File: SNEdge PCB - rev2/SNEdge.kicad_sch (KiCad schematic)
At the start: 37 parts, among them J10 R_O, J2 R_E, J3 B_E, J4 G_E, J5 G_IN, J6 B_IN, J7 R_IN, J8 G_O, J9 B_O, U1 THS7374, U3 MIC5205-5.0YM5

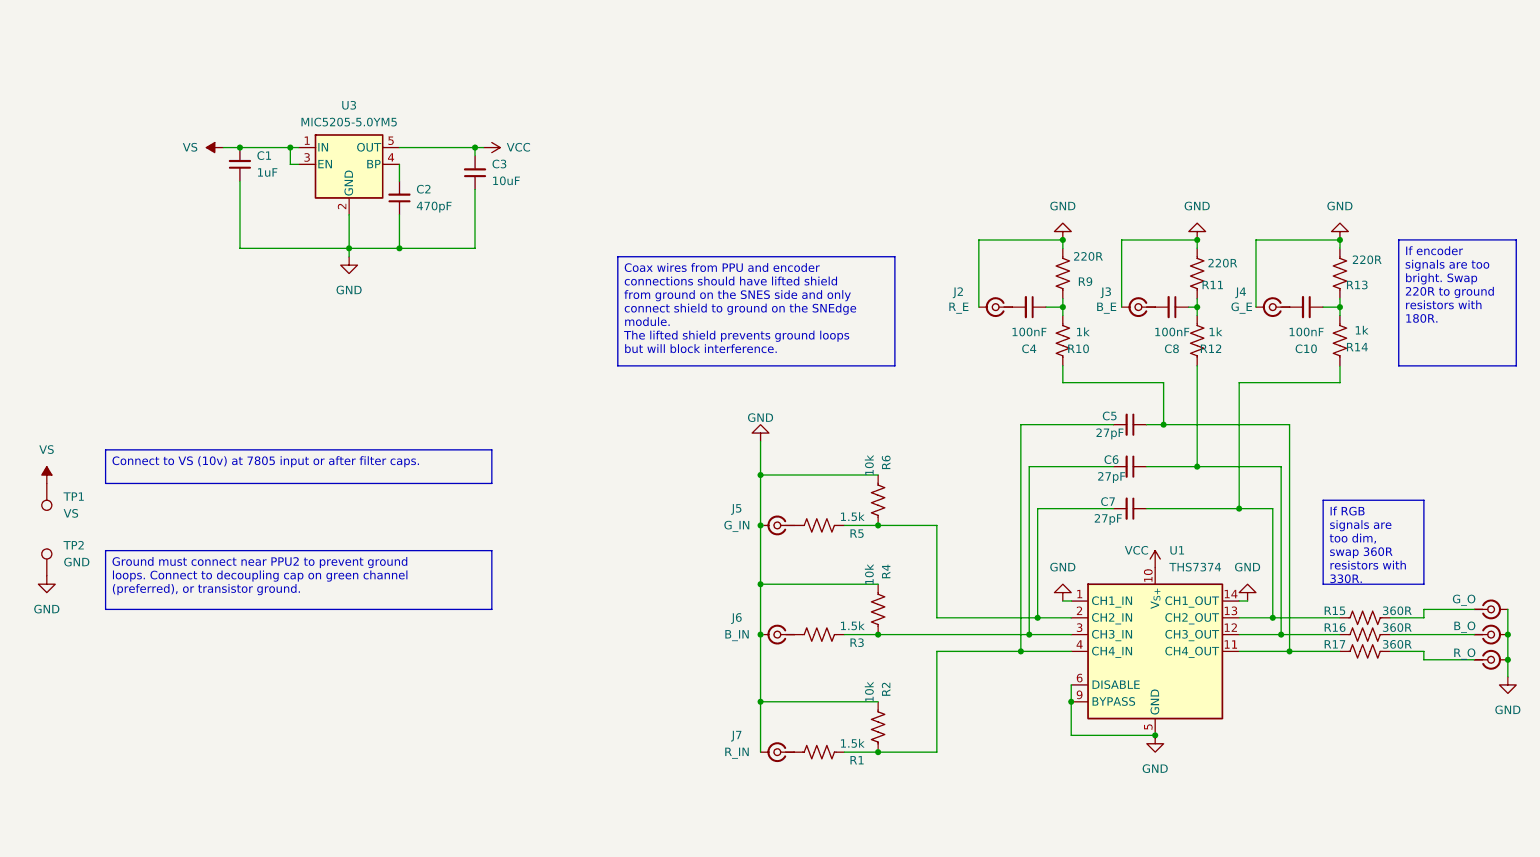
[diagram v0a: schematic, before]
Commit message: v2.1 remove voltage divider and voltage regulator, input pull down and power filtering
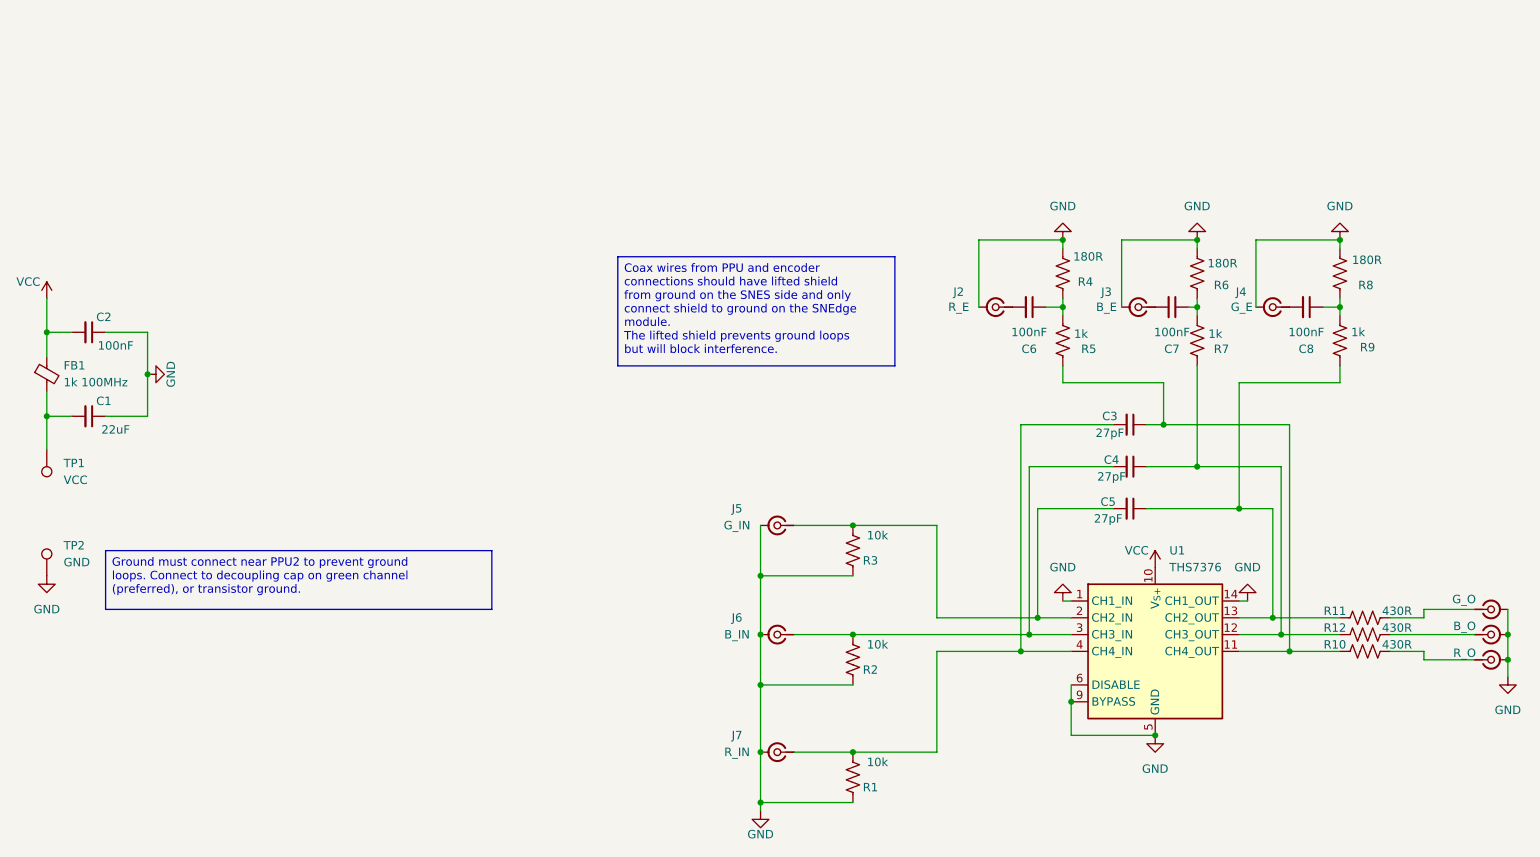
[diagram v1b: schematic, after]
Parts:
- removed C3: 10uF, Capacitor_SMD:C_0805_2012Metric_Pad1.18x1.45mm_HandSolder, symbol Device:C_Small
- removed R4, R6: 10k, Resistor_SMD:R_0805_2012Metric_Pad1.20x1.40mm_HandSolder, symbol Device:R_US
- removed R5: 1.5k, Resistor_SMD:R_0805_2012Metric_Pad1.20x1.40mm_HandSolder, symbol Device:R_US
- removed U3: MIC5205-5.0YM5, Package_TO_SOT_SMD:SOT-23-5, symbol Regulator_Linear:MIC5205-5.0YM5
- added FB1: 1k 100MHz, Resistor_SMD:R_0805_2012Metric_Pad1.20x1.40mm_HandSolder, symbol Device:FerriteBead_Small
- C1: value 1uF -> 22uF
- C2: value 470pF -> 100nF
- R1, R3: value 1.5k -> 10k
- R10: renamed from R17; value 360R -> 430R
- R11: renamed from R15; value 360R -> 430R
- R12: renamed from R16; value 360R -> 430R
- R4: renamed from R9; value 220R -> 180R
- R6: renamed from R11; value 220R -> 180R
- R8: renamed from R13; value 220R -> 180R
- TP1: value VS -> VCC
- U1: value THS7374 -> THS7376
- renumbered C5 to C3, C6 to C4, C7 to C5, C4 to C6, C8 to C7, C10 to C8, R10 to R5, R12 to R7, R14 to R9
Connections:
- net GND: now also R1.1, R2.1, R3.1; no longer R2.2
- net VCC: now also C2.2, FB1.1
- net at C5.2, U1.2 (CH2_IN): now also J5.1 (In), R3.2
- net at C4.2, U1.3 (CH3_IN): now also J6.1 (In), R2.2; no longer R3.2
- net at C3.2, R1.2, U1.4 (CH4_IN): now also J7.1 (In); no longer R2.1
- net VS: no longer names the net of C1.2, TP1.1
- net VS: now also FB1.2
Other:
- moved on the sheet: TP1

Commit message: Refactor for purity
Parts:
- removed C6, C7, C8: 100nF, Capacitor_SMD:C_0805_2012Metric_Pad1.18x1.45mm_HandSolder, symbol Device:C_Small
- removed J2: R_E, Connector_Coaxial:U.FL_Hirose_U.FL-R-SMT-1_Vertical, symbol Connector:Conn_Coaxial_Small
- removed J3: B_E, Connector_Coaxial:U.FL_Hirose_U.FL-R-SMT-1_Vertical, symbol Connector:Conn_Coaxial_Small
- removed J4: G_E, Connector_Coaxial:U.FL_Hirose_U.FL-R-SMT-1_Vertical, symbol Connector:Conn_Coaxial_Small
- removed J5: G_IN, Connector_Coaxial:U.FL_Hirose_U.FL-R-SMT-1_Vertical, symbol Connector:Conn_Coaxial_Small
- removed J6: B_IN, Connector_Coaxial:U.FL_Hirose_U.FL-R-SMT-1_Vertical, symbol Connector:Conn_Coaxial_Small
- removed J7: R_IN, Connector_Coaxial:U.FL_Hirose_U.FL-R-SMT-1_Vertical, symbol Connector:Conn_Coaxial_Small
- added TP3: G_IN, TestPoint:TestPoint_Pad_1.5x1.5mm, symbol Connector:TestPoint
- added TP4: B_IN, TestPoint:TestPoint_Pad_1.5x1.5mm, symbol Connector:TestPoint
- added TP5: R_IN, TestPoint:TestPoint_Pad_1.5x1.5mm, symbol Connector:TestPoint
- added TP6: R_E, TestPoint:TestPoint_Pad_1.5x1.5mm, symbol Connector:TestPoint
- added TP7: B_E, TestPoint:TestPoint_Pad_1.5x1.5mm, symbol Connector:TestPoint
- added TP8: G_E, TestPoint:TestPoint_Pad_1.5x1.5mm, symbol Connector:TestPoint
- R4, R6, R8: value 180R -> 75R
- R5, R7, R9: value 1k -> 430R
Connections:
- net at R4.1, R5.2: now also TP6.1
- net at C5.2, R3.2, U1.2 (CH2_IN): now also TP3.1
- net at C4.2, R2.2, U1.3 (CH3_IN): now also TP4.1
- net at C3.2, R1.2, U1.4 (CH4_IN): now also TP5.1
- net at R8.1, R9.2: now also TP8.1
- net at R6.1, R7.2: now also TP7.1
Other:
- moved on the sheet: R4, R6, R8

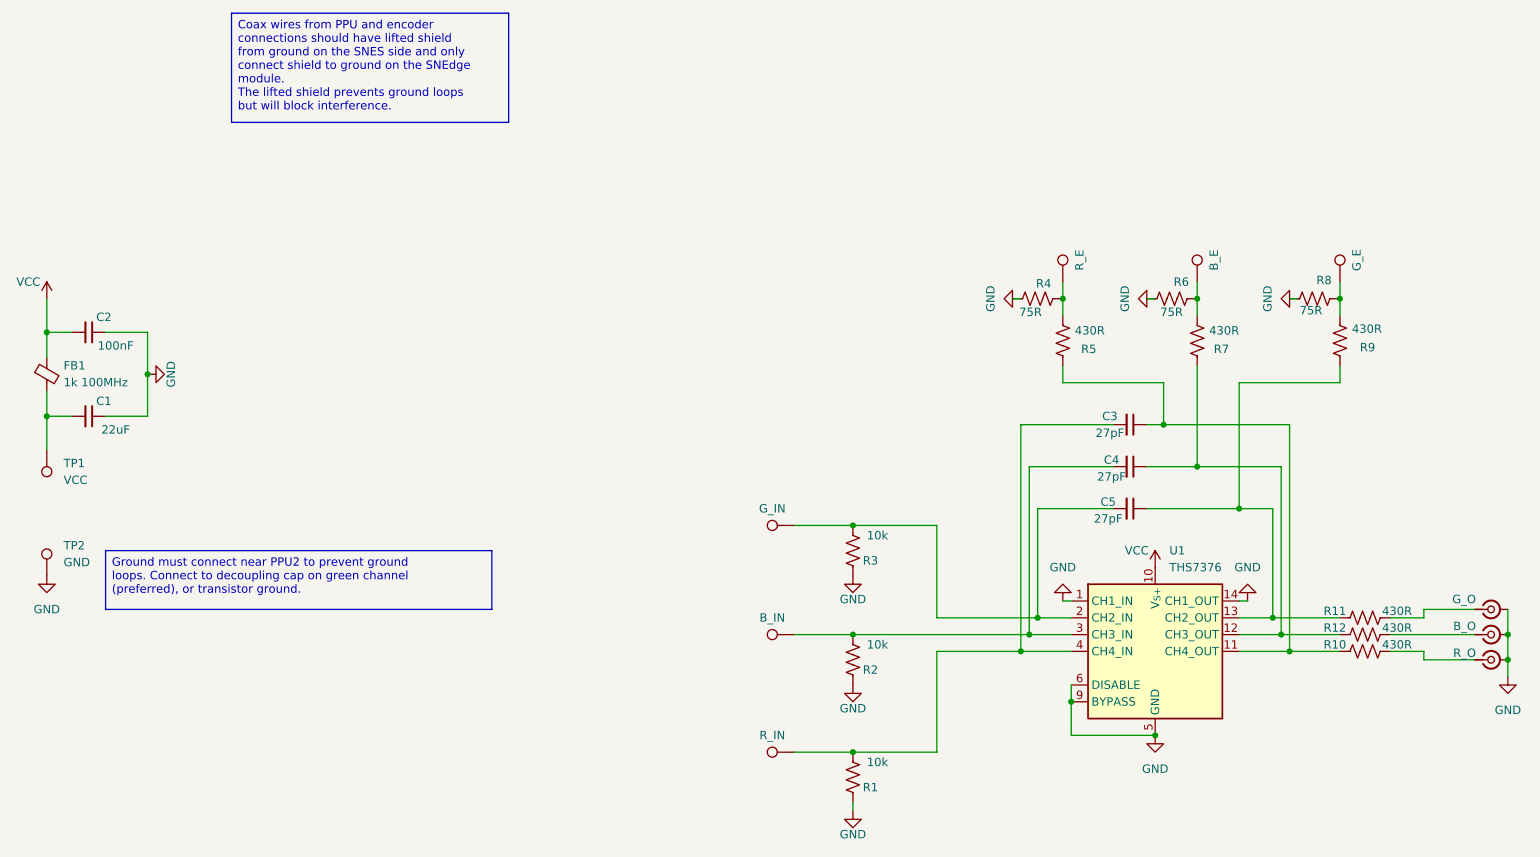
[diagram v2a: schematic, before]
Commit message: Add encoder coupling capacitors back
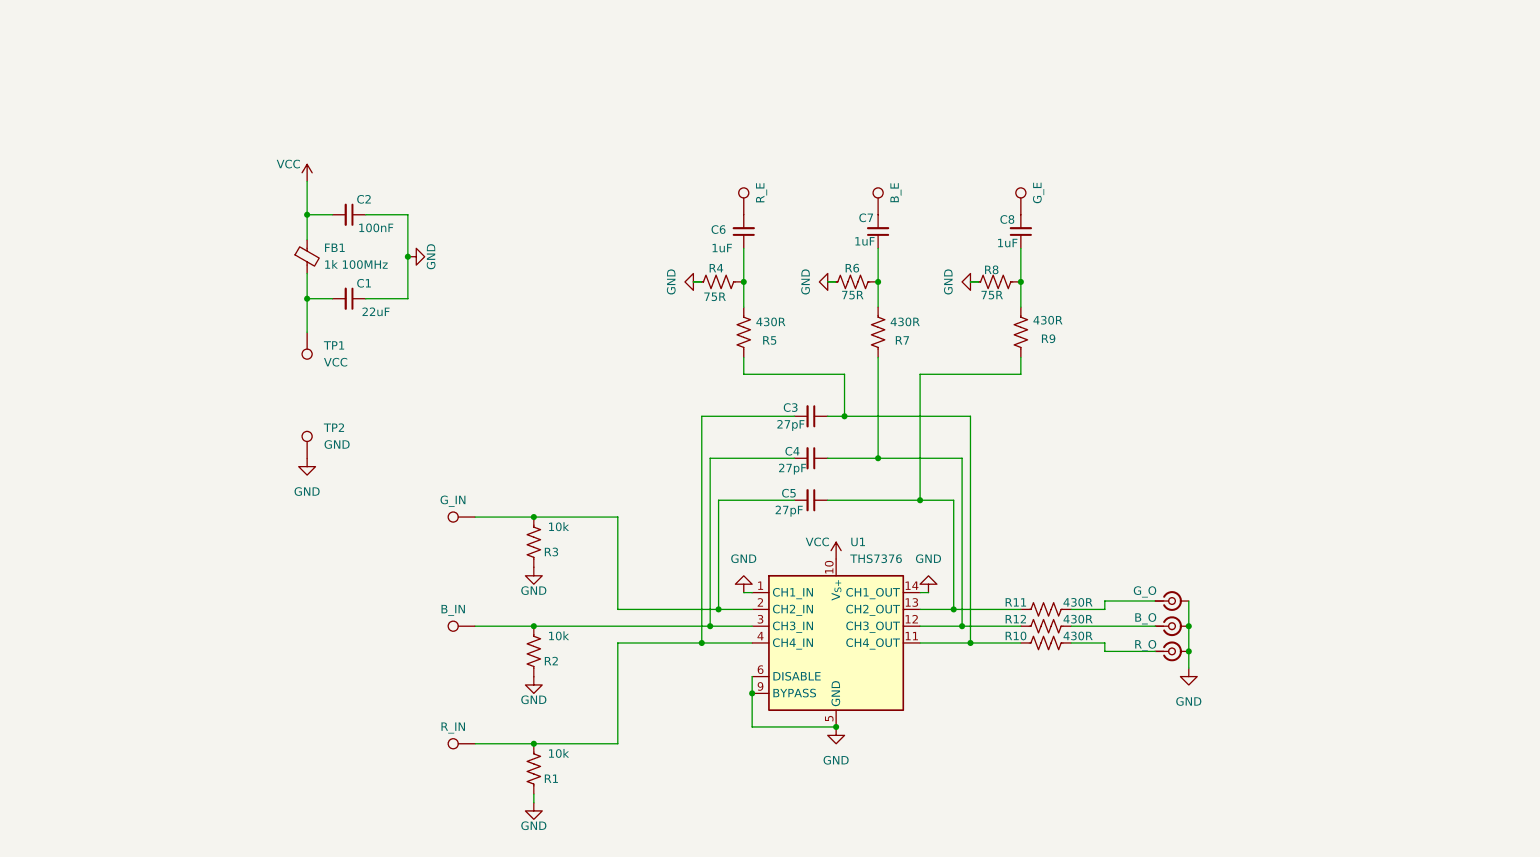
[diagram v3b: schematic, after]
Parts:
- added C6, C7, C8: 1uF, Capacitor_SMD:C_0805_2012Metric_Pad1.18x1.45mm_HandSolder, symbol Device:C_Small
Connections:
- net at R8.1, R9.2: now also C8.1; no longer TP8.1
- net at R6.1, R7.2: now also C7.1; no longer TP7.1
- net at R4.1, R5.2: now also C6.1; no longer TP6.1
- new net: C6.2, TP6.1
- new net: C7.2, TP7.1
- new net: C8.2, TP8.1
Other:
- moved on the sheet: C1, C2, C3, C4, C5, FB1, R1, R10, R11, R12, R2, R3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

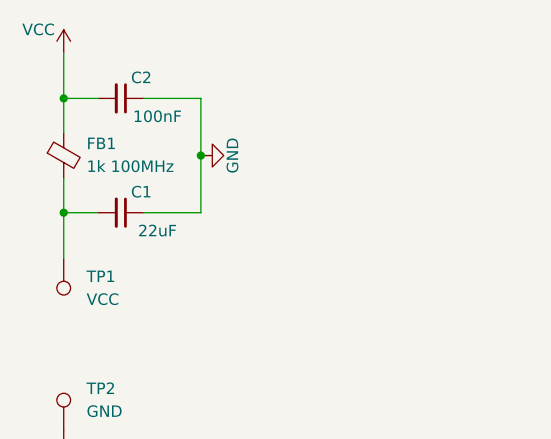
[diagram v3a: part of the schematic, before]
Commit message: Switch position of ferrite bead and bulk capacitor
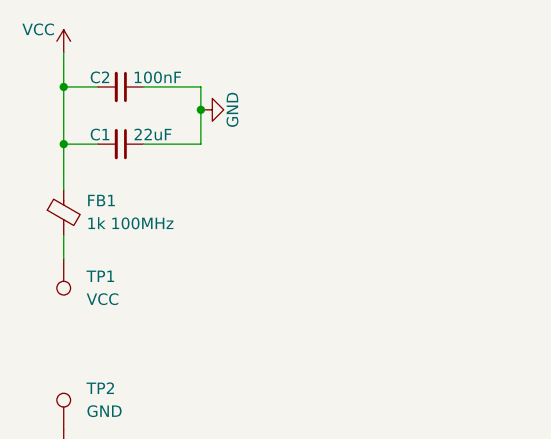
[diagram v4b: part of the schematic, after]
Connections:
- net VCC: now also C1.2
- net at FB1.2, TP1.1: no longer C1.2
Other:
- moved on the sheet: C1, C2, FB1
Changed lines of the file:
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@@
-	)
-	(junction
-		(at 68.58 58.42)
-		(diameter 0)
-		(color 0 0 0 0)
 	)
 	(junction
@@
 	)
 	(junction
+		(at 68.58 44.45)
+		(diameter 0)
+		(color 0 0 0 0)
+	)
+	(junction
 		(at 161.29 88.9)
 		(diameter 0)
@@
 	)
 	(junction
-		(at 68.58 45.72)
-		(diameter 0)
-		(color 0 0 0 0)
-	)
-	(junction
-		(at 83.82 52.07)
+		(at 68.58 50.8)
 		(diameter 0)
 		(color 0 0 0 0)
@@
 		(color 0 0 0 0)
 	)
+	(junction
+		(at 83.82 46.99)
+		(diameter 0)
+		(color 0 0 0 0)
+	)
 	(wire
 		(pts
@@
 	(wire
 		(pts
-			(xy 68.58 58.42) (xy 72.39 58.42)
+			(xy 68.58 50.8) (xy 72.39 50.8)
 		)
 		(stroke
@@
 	(wire
 		(pts
-			(xy 68.58 54.61) (xy 68.58 58.42)
-		)
-		(stroke
-			(width 0)
-			(type default)
-		)
-	)
-	(wire
-		(pts
 			(xy 115.57 110.49) (xy 115.57 125.73)
 		)
@@
 	(wire
 		(pts
-			(xy 83.82 58.42) (xy 83.82 52.07)
+			(xy 83.82 46.99) (xy 83.82 50.8)
 		)
 		(stroke
@@
 	(wire
 		(pts
+			(xy 68.58 60.96) (xy 68.58 63.5)
+		)
+		(stroke
+			(width 0)
+			(type default)
+		)
+	)
+	(wire
+		(pts
 			(xy 147.32 76.2) (xy 149.86 76.2)
 		)
@@
 	(wire
 		(pts
-			(xy 72.39 45.72) (xy 68.58 45.72)
+			(xy 72.39 44.45) (xy 68.58 44.45)
 		)
 		(stroke
@@
 	(wire
 		(pts
-			(xy 83.82 45.72) (xy 83.82 52.07)
+			(xy 83.82 44.45) (xy 83.82 46.99)
+		)
+		(stroke
+			(width 0)
+			(type default)
+		)
+	)
+	(wire
+		(pts
+			(xy 68.58 50.8) (xy 68.58 55.88)
 		)
 		(stroke
@@
 	(wire
 		(pts
-			(xy 68.58 49.53) (xy 68.58 45.72)
-		)
-		(stroke
-			(width 0)
-			(type default)
-		)
-	)
-	(wire
-		(pts
 			(xy 135.89 118.11) (xy 135.89 123.19)
 		)
@@
 	(wire
 		(pts
-			(xy 68.58 58.42) (xy 68.58 63.5)
-		)
-		(stroke
-			(width 0)
-			(type default)
-		)
-	)
-	(wire
-		(pts
 			(xy 147.32 82.55) (xy 154.94 82.55)
 		)
@@
 	(wire
 		(pts
-			(xy 68.58 40.64) (xy 68.58 45.72)
-		)
-		(stroke
-			(width 0)
-			(type default)
-		)
-	)
-	(wire
-		(pts
-			(xy 77.47 45.72) (xy 83.82 45.72)
+			(xy 68.58 40.64) (xy 68.58 44.45)
+		)
+		(stroke
+			(width 0)
+			(type default)
+		)
+	)
+	(wire
+		(pts
+			(xy 77.47 44.45) (xy 83.82 44.45)
 		)
 		(stroke
@@
 	(wire
 		(pts
+			(xy 68.58 44.45) (xy 68.58 50.8)
+		)
+		(stroke
+			(width 0)
+			(type default)
+		)
+	)
+	(wire
+		(pts
 			(xy 184.15 110.49) (xy 189.23 110.49)
 		)
@@
 	(wire
 		(pts
-			(xy 77.47 58.42) (xy 83.82 58.42)
+			(xy 77.47 50.8) (xy 83.82 50.8)
 		)
 		(stroke
@@
 	(symbol
 		(lib_id "power:GND")
-		(at 83.82 52.07 90)
+		(at 83.82 46.99 90)
 		(unit 1)
 		(exclude_from_sim no)
@@
 		(dnp no)
 		(property "Reference" "#PWR03"
-			(at 90.17 52.07 0)
+			(at 90.17 46.99 0)
 			(effects
 				(font
@@
 		)
 		(property "Value" "GND"
-			(at 87.376 52.07 0)
+			(at 87.376 46.99 0)
 			(effects
 				(font
@@
 		)
 		(property "Footprint" ""
-			(at 83.82 52.07 0)
+			(at 83.82 46.99 0)
 			(effects
 				(font
@@
 		)
 		(property "Datasheet" ""
-			(at 83.82 52.07 0)
+			(at 83.82 46.99 0)
 			(effects
 				(font
@@
 		)
 		(property "Description" "Power symbol creates a global label with name \"GND\" , ground"
-			(at 83.82 52.07 0)
+			(at 83.82 46.99 0)
 			(effects
 				(font
@@
 	(symbol
 		(lib_id "Device:C_Small")
-		(at 74.93 58.42 270)
+		(at 74.93 50.8 270)
 		(unit 1)
 		(exclude_from_sim no)
@@
 		(dnp no)
 		(property "Reference" "C1"
-			(at 77.216 56.134 90)
+			(at 72.644 49.784 90)
 			(effects
 				(font
@@
 		)
 		(property "Value" "22uF"
-			(at 78.994 60.452 90)
+			(at 78.486 49.784 90)
 			(effects
 				(font
@@
 		)
 		(property "Footprint" "Capacitor_SMD:C_0805_2012Metric_Pad1.18x1.45mm_HandSolder"
-			(at 74.93 58.42 0)
+			(at 74.93 50.8 0)
 			(effects
 				(font
@@
 		)
 		(property "Datasheet" "~"
-			(at 74.93 58.42 0)
+			(at 74.93 50.8 0)
 			(effects
 				(font
@@
 		)
 		(property "Description" "Unpolarized capacitor, small symbol"
-			(at 74.93 58.42 0)
+			(at 74.93 50.8 0)
 			(effects
 				(font
@@
 		)
 		(property "Digi_PN" ""
-			(at 74.93 58.42 0)
+			(at 74.93 50.8 0)
 			(effects
 				(font
@@
 		)
 		(property "MFG_PN" ""
-			(at 74.93 58.42 0)
+			(at 74.93 50.8 0)
 			(effects
 				(font
@@
 	(symbol
 		(lib_id "Device:C_Small")
-		(at 74.93 45.72 270)
+		(at 74.93 44.45 270)
 		(unit 1)
 		(exclude_from_sim no)
@@
 		(dnp no)
 		(property "Reference" "C2"
-			(at 77.216 43.434 90)
+			(at 72.644 43.434 90)
 			(effects
 				(font
@@
 		)
 		(property "Value" "100nF"
-			(at 78.994 47.752 90)
+			(at 78.994 43.434 90)
 			(effects
 				(font
@@
 		)
 		(property "Footprint" "Capacitor_SMD:C_0805_2012Metric_Pad1.18x1.45mm_HandSolder"
-			(at 74.93 45.72 0)
+			(at 74.93 44.45 0)
 			(effects
 				(font
@@
 		)
 		(property "Datasheet" "~"
-			(at 74.93 45.72 0)
+			(at 74.93 44.45 0)
 			(effects
 				(font
@@
 		)
 		(property "Description" "Unpolarized capacitor, small symbol"
-			(at 74.93 45.72 0)
+			(at 74.93 44.45 0)
 			(effects
 				(font
@@
 		)
 		(property "Digi_PN" ""
-			(at 74.93 45.72 0)
+			(at 74.93 44.45 0)
 			(effects
 				(font
@@
 		)
 		(property "MFG_PN" ""
-			(at 74.93 45.72 0)
+			(at 74.93 44.45 0)
 			(effects
 				(font
@@
 	(symbol
 		(lib_id "Device:FerriteBead_Small")
-		(at 68.58 52.07 0)
+		(at 68.58 58.42 0)
 		(unit 1)
 		(exclude_from_sim no)
@@
 		(fields_autoplaced yes)
 		(property "Reference" "FB1"
-			(at 71.12 50.7618 0)
+			(at 71.12 57.1118 0)
 			(effects
 				(font
@@
 		)
 		(property "Value" "1k 100MHz"
-			(at 71.12 53.3018 0)
+			(at 71.12 59.6518 0)
 			(effects
 				(font
@@
 		)
 		(property "Footprint" "Resistor_SMD:R_0805_2012Metric_Pad1.20x1.40mm_HandSolder"
-			(at 66.802 52.07 90)
+			(at 66.802 58.42 90)
 			(effects
 				(font
@@
 		)
 		(property "Datasheet" "~"
-			(at 68.58 52.07 0)
+			(at 68.58 58.42 0)
 			(effects
 				(font
@@
 		)
 		(property "Description" "Ferrite bead, small symbol"
-			(at 68.58 52.07 0)
-			(effects
-				(font
+			(at 68.58 58.42 0)
+			(effects
+				(font
